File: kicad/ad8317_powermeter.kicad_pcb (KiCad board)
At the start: 4 copper layers, 88 x 34 mm, 69 parts, among them J1 Conn_Coaxial, J2 USB_C_Receptacle_USB2.0_16P, J3 Conn_01x04_Pin, J4 Conn_01x02_Pin, J5 Conn_ARM_JTAG_SWD_10_UART, SW1 SW_Omron_B3FS, SW2 SW_Omron_B3FS, U1 AD8317, U2 STM32F373RCTx, U3 REF3030, U4 ADP150AUJZ-3.3-R7, U5 BQ24092DGQ, U6 AP2112K-3.3, U7 M24C02-WMN

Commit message: Commit all current changes
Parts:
- moved C6 10.5 mm to (147.7, 87.6), turned to 0 degrees
- moved U5 8.49 mm to (201.2, 76.0)
- moved J4 5.48 mm to (210.1, 75.1)
- moved R5 3.54 mm to (149.6, 81.4), turned to -90 degrees
- moved C4 3.04 mm to (147.8, 80.9), turned to 180 degrees
- moved C27 2.81 mm to (204.7, 78.2), turned to 90 degrees
- moved C5 2.28 mm to (147.7, 81.9), turned to 180 degrees
- moved C25 0.65 mm to (205.8, 78.2), turned to -90 degrees
- turned REF** to 180 degrees
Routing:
- net GND: track 9.74 -> 18.0 mm, vias 0 -> 4
- net Net-(U2-PB2): track 0.00 -> 3.03 mm
- net Net-(U1-VOUT): track 0.00 -> 2.89 mm
- net Net-(U1-TADJ): track 0.00 -> 2.86 mm
- net /MCU/+3V3_A: track 0.00 -> 2.69 mm
- net Net-(U1-CLPF): track 0.00 -> 2.40 mm
- net Net-(U1-VSET): track 0.00 -> 1.91 mm
- net Net-(J1-In): track 5.52 -> 7.01 mm
- net /MCU/VDET: track 0.00 -> 1.05 mm
- added copper zone on In2.Cu, net /MCU/+3V3
- added copper zone on In1.Cu, net GND
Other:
- outline, holes or cut-outs redrawn
- board text added: "CREEPAGE: 17.73mm (req 0.16mm) PASS EXTRA_LOW_VOLTAGE-GROUND, 0 waypoints +5V ↔ GND"

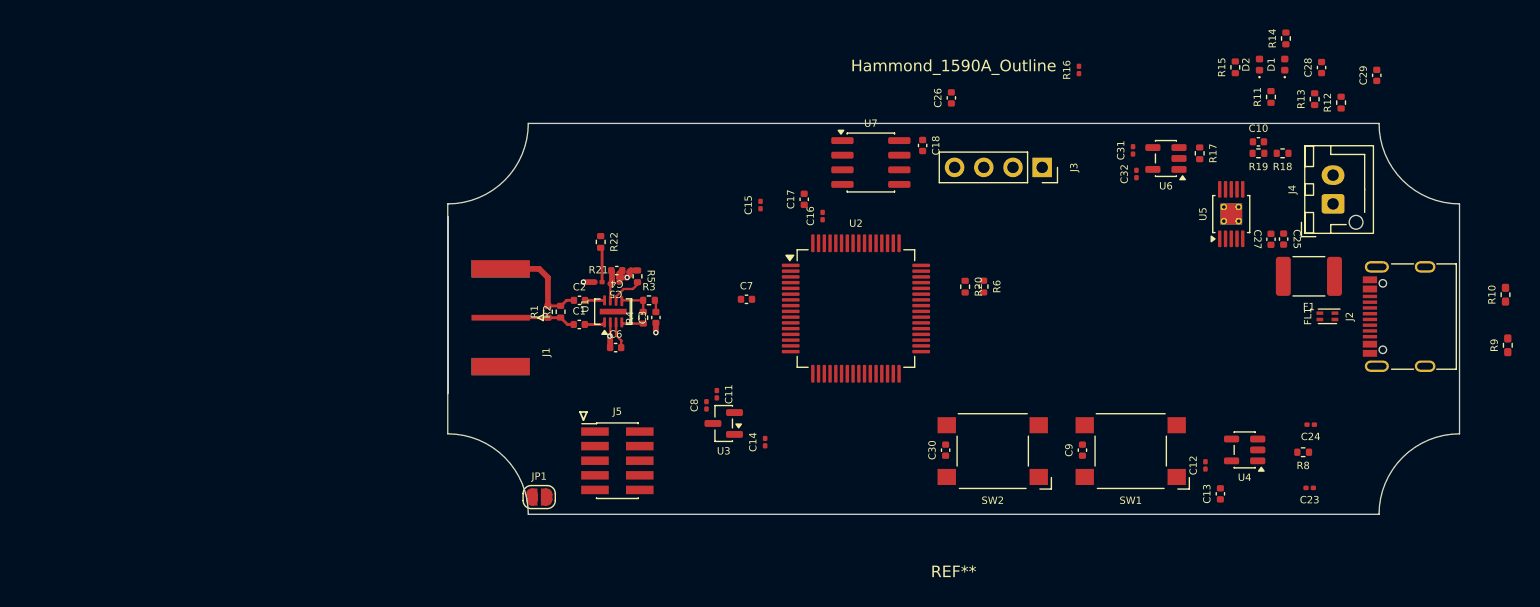
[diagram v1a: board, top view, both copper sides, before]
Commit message: Refine EMerge labels/colors and passive naming; sync artifact set
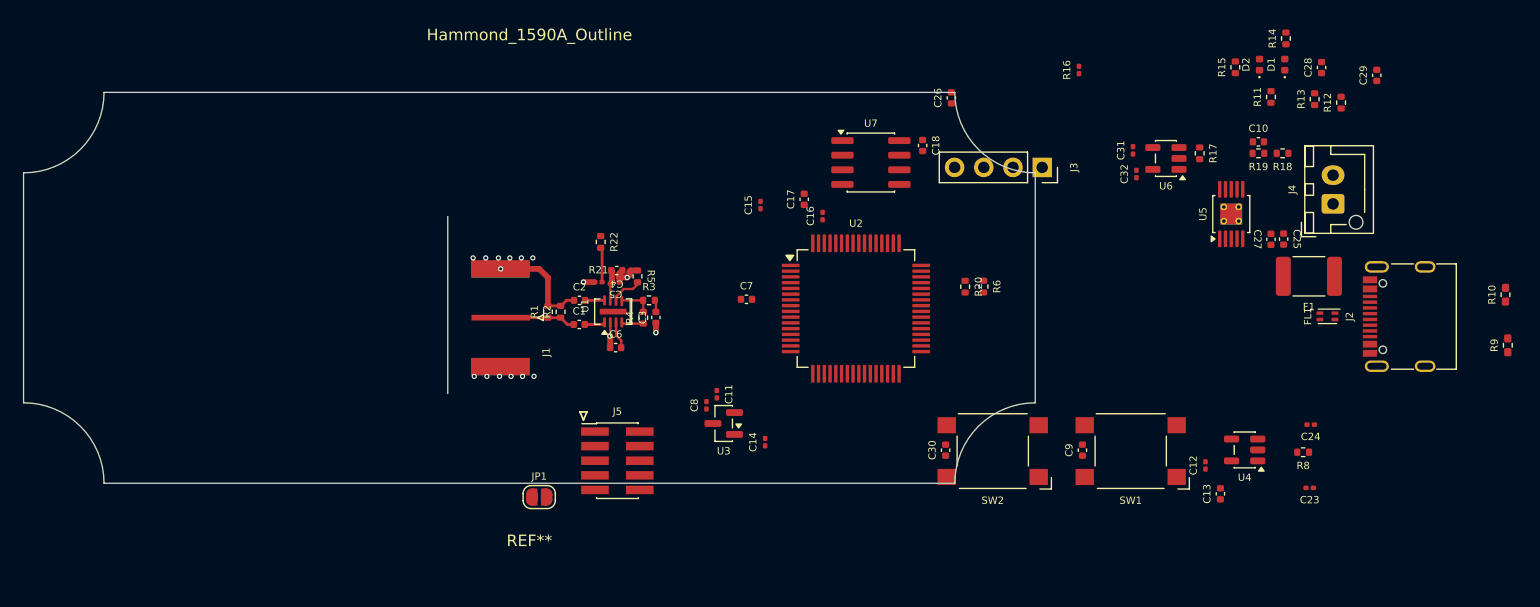
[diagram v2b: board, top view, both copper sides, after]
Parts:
- moved REF** 37.0 mm to (140.2, 82.4)
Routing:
- net GND: vias 4 -> 17
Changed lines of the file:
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@@
 	(footprint "ad8317_custom:Hammond_1590A_Board_Outline"
 		(layer "F.Cu")
-		(at 177.1 85.1 180)
+		(at 140.2 82.4 180)
 		(descr "Mechanical PCB outline for Hammond 1590A — 88x34mm with R7mm concave corner notches clearing mounting bosses (0.5mm clearance from 89x35mm internal void)")
 		(tags "mechanical outline enclosure hammond 1590a")
@@
 	)
 	(via
+		(at 136.4 79.8)
+		(size 0.4572)
+		(drill 0.254)
+		(layers "F.Cu" "B.Cu")
+		(net "GND")
+	)
+	(via
+		(at 139.6 90.1)
+		(size 0.4572)
+		(drill 0.254)
+		(layers "F.Cu" "B.Cu")
+		(net "GND")
+	)
+	(via
+		(at 136.5 90.1)
+		(size 0.4572)
+		(drill 0.254)
+		(layers "F.Cu" "B.Cu")
+		(net "GND")
+	)
+	(via
+		(at 138.6 90.1)
+		(size 0.4572)
+		(drill 0.254)
+		(layers "F.Cu" "B.Cu")
+		(net "GND")
+	)
+	(via
+		(at 137.5 79.8)
+		(size 0.4572)
+		(drill 0.254)
+		(layers "F.Cu" "B.Cu")
+		(net "GND")
+	)
+	(via
 		(at 148.7 81.5)
+		(size 0.4572)
+		(drill 0.254)
+		(layers "F.Cu" "B.Cu")
+		(net "GND")
+	)
+	(via
+		(at 137.7 80.75)
+		(size 0.4572)
+		(drill 0.254)
+		(layers "F.Cu" "B.Cu")
+		(net "GND")
+	)
+	(via
+		(at 139.5 79.8)
 		(size 0.4572)
 		(drill 0.254)
@@
 	)
 	(via
+		(at 138.5 79.8)
+		(size 0.4572)
+		(drill 0.254)
+		(layers "F.Cu" "B.Cu")
+		(net "GND")
+	)
+	(via
+		(at 137.6 90.1)
+		(size 0.4572)
+		(drill 0.254)
+		(layers "F.Cu" "B.Cu")
+		(net "GND")
+	)
+	(via
 		(at 144.9 81.9)
 		(size 0.4572)
@@
 		(net "GND")
 	)
+	(via
+		(at 140.5 79.8)
+		(size 0.4572)
+		(drill 0.254)
+		(layers "F.Cu" "B.Cu")
+		(free yes)
+		(net "GND")
+	)
+	(via
+		(at 135.4 90.1)
+		(size 0.4572)
+		(drill 0.254)
+		(layers "F.Cu" "B.Cu")
+		(net "GND")
+	)
+	(via
+		(at 135.3 79.8)
+		(size 0.4572)
+		(drill 0.254)
+		(layers "F.Cu" "B.Cu")
+		(net "GND")
+	)
+	(via
+		(at 140.6 90.1)
+		(size 0.4572)
+		(drill 0.254)
+		(layers "F.Cu" "B.Cu")
+		(free yes)
+		(net "GND")
+	)

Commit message: Use Würth 60312202114307 SMA connector
Replace J1 with the shorter Würth WR-SMA connector, add its footprint and 3D model, make KiCad library paths portable, and include the reviewed EMerge geometry/export updates. Generated results and private local paths are intentionally excluded.
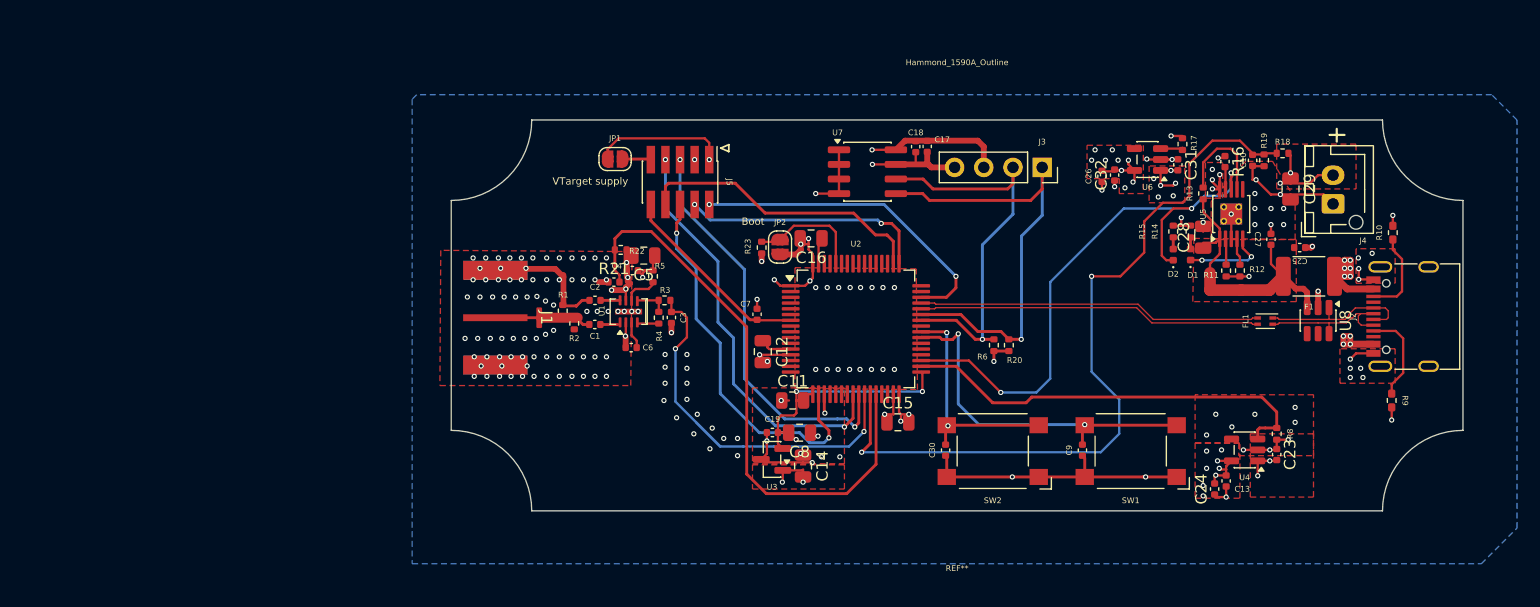
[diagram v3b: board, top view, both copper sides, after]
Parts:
- added C19: 100nF, Capacitor_SMD:C_0402_1005Metric, F.Cu at (161.3, 95.0)
- added JP2: Boot0, Jumper:SolderJumper-2_P1.3mm_Open_RoundedPad1.0x1.5mm, F.Cu at (162.0, 78.8)
- added R23: 10K, Resistor_SMD:R_0402_1005Metric, F.Cu at (160.4, 78.9)
- added U8: TPD4E1U06, Package_TO_SOT_SMD:SOT-23-6, F.Cu at (208.8, 85.2)
- C11, C12, C14, C15, C16, C5, C8: footprint Capacitor_SMD:C_0201_0603Metric -> Capacitor_SMD:C_0805_2012Metric
- C23, C24, C31, C32, R16, R21: footprint Capacitor_SMD:C_0201_0603Metric -> Capacitor_SMD:C_0402_1005Metric
- C28, C29: footprint Capacitor_SMD:C_0402_1005Metric -> Capacitor_SMD:C_0805_2012Metric
- J1: value Conn_Coaxial -> 60312202114307; footprint Connector_Coaxial:SMA_Amphenol_132289_EdgeMount -> Connector_SMD_Wurth:J_Wurth_WR-SMA_60312202114307
- moved C12 39.8 mm to (160.5, 88.0), turned to -90 degrees
- moved REF** 37.3 mm to (177.4, 84.8)
- moved JP1 30.1 mm to (147.7, 71.2)
- moved J5 24.8 mm to (153.3, 73.2), turned to -90 degrees
- moved C15 22.4 mm to (172.2, 94.1), turned to 0 degrees
- moved R14 18.7 mm to (197.7, 77.5)
- moved D1 18.4 mm to (197.7, 79.5)
- moved D2 18.2 mm to (196.2, 79.5)
- moved C28 18.0 mm to (198.8, 78.0)
- moved R12 17.1 mm to (202.0, 80.9)
- moved R11 15.6 mm to (200.8, 80.9), turned to -90 degrees
- moved R15 15.3 mm to (196.2, 77.5)
- moved R16 15.0 mm to (200.7, 71.4), turned to -90 degrees
- moved C26 14.8 mm to (190.0, 72.7)
- moved R13 12.7 mm to (198.8, 74.2)
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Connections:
- D2 pad 1: /Power_Management/CHG_STAT -> /MCU/CHG_STAT
- FL1 pad 1: Net-(FL1-Pad1) -> /User_Interface/USB_D1P
- FL1 pad 2: /MCU/USB_DM -> /MCU/USB_DP
- FL1 pad 3: /MCU/USB_DP -> /MCU/USB_DN
- FL1 pad 4: Net-(FL1-Pad4) -> /User_Interface/USB_D1N
- J2 pad A6: Net-(FL1-Pad4) -> /User_Interface/USB_D1P
- J2 pad A7: Net-(FL1-Pad1) -> /User_Interface/USB_D1N
- J2 pad B6: Net-(FL1-Pad4) -> /User_Interface/USB_D1P
- J2 pad B7: Net-(FL1-Pad1) -> /User_Interface/USB_D1N
- J3 pad 3: GND -> /MCU/+3V3
- J3 pad 4: /MCU/+3V3 -> GND
- U2 pad 34: unconnected-(U2-PB14-Pad34) -> /MCU/ANALOG_PWR
- U2 pad 35: unconnected-(U2-PB15-Pad35) -> /MCU/CHG_STAT
- U2 pad 44: /MCU/USB_DM -> /MCU/USB_DN
- U2 pad 60: unconnected-(U2-BOOT0-Pad60) -> Net-(JP2-A)
- U2 pad 8: /MCU/ANALOG_PWR -> unconnected-(U2-PC0-Pad8)
- U2 pad 9: /MCU/CHG_STAT -> unconnected-(U2-PC1-Pad9)
- U5 pad 8: /Power_Management/CHG_STAT -> /MCU/CHG_STAT
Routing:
- net GND: track 18.0 -> 121.1 mm, vias 17 -> 169
- net Net-(U2-PB1): track 0.00 -> 67.9 mm, vias 0 -> 2
- net /MCU/CHG_STAT: track 0.00 -> 50.5 mm, vias 0 -> 3
- net /MCU/+3V3: track 0.00 -> 49.1 mm, vias 0 -> 19
- net Net-(U2-PB2): track 3.03 -> 51.0 mm
- net /MCU/I2C_SDA: track 0.00 -> 40.6 mm, vias 0 -> 1
- net /MCU/ANALOG_PWR: track 0.00 -> 36.9 mm
- net /MCU/UART_RX: track 0.00 -> 36.3 mm, vias 0 -> 2
- net /MCU/UART_TX: track 0.00 -> 35.7 mm, vias 0 -> 2
- net /MCU/I2C_SCL: track 0.00 -> 35.2 mm, vias 0 -> 1
- net /MCU/VDET: track 1.05 -> 35.0 mm, vias 0 -> 2
- net /MCU/JTAG_TDO: track 0.00 -> 33.7 mm, vias 0 -> 2
- net Net-(U2-PC8): track 0.00 -> 31.1 mm, vias 0 -> 2
- net /MCU/USB_DP: track 0.00 -> 29.9 mm
- net /MCU/USB_DN: track 0.00 -> 29.9 mm
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- added copper zone on F.Cu, net +5V
- added copper zone on F.Cu, net /MCU/+3V3
- added copper zone on F.Cu, net /MCU/+3V3_A
- added copper zone on In2.Cu, net /MCU/+3V3_A
- added copper zone on F.Cu, net /MCU/VBAT
- added copper zone on In2.Cu, net /MCU/VBAT
- added copper zone on B.Cu, net GND
- added copper zone on F.Cu, net GND
- added copper zone on In2.Cu, net Net-(F1-Pad1)
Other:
- board text added: "Boot"
- board text added: "VTarget supply"
- board text removed: "CREEPAGE: 17.73mm (req 0.16mm) PASS EXTRA_LOW_VOLTAGE-GROUND, 0 waypoints +5V ↔ GND"
